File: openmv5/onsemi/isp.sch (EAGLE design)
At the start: 58 parts, among them IC1 AP0202AT2L00XPGA0, IC2 MIC5365-2.8YC5-TR, IC3 TLV62568PDDCR, J1 DF12-36-DS, J2 DF12-36-DP, M1 9774030151R, M2 9774030151R, Q1 PMXB120EPEZ

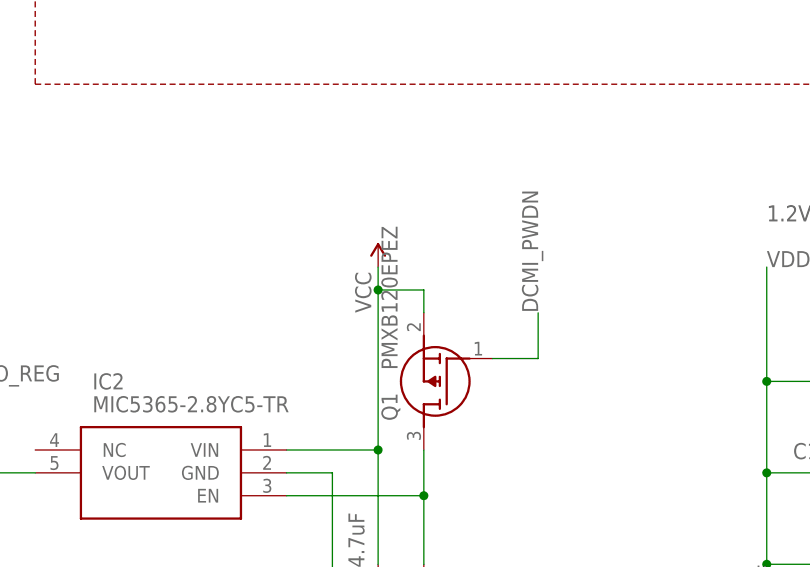
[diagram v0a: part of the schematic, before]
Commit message: Update camera modules to use different non-flippable pmosfet
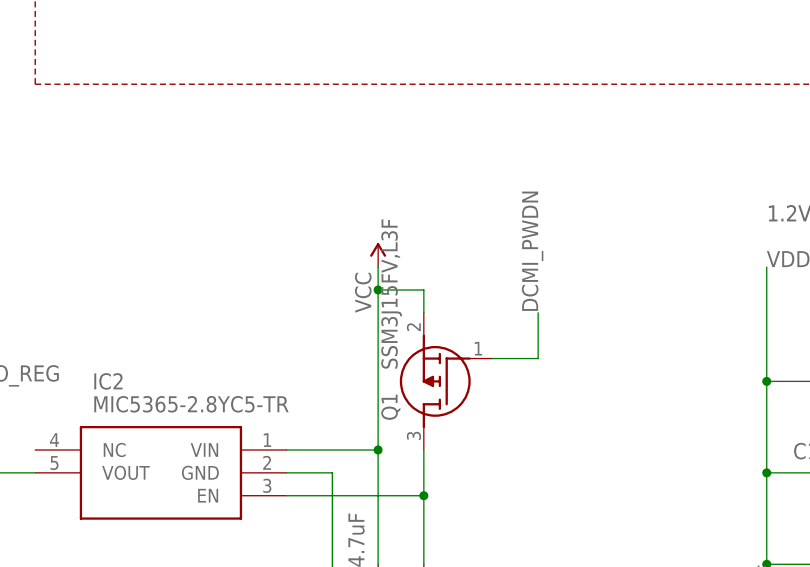
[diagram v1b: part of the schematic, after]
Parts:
- J1: MPN DF12NB-36DS-0.5V(51) -> DF12NB(3.0)-36DS-0.5V(51)
- Q1: value PMXB120EPEZ -> SSM3J15FV,L3F; device PMXB120EPEZ:PMXB120EPEZ -> SSM3J15FV_L3F:SSM3J15FV,L3F; MPN PMXB120EPEZ -> SSM3J15FV,L3F
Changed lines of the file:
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@@
 </part>
 <part name="GND11" library="supply" deviceset="GND" device=""/>
-<part name="Q1" library="PMXB120EPEZ" deviceset="PMXB120EPEZ" device="">
-<attribute name="MPN" value="PMXB120EPEZ"/>
+<part name="Q1" library="SSM3J15FV_L3F" deviceset="SSM3J15FV,L3F" device="">
+<attribute name="MPN" value="SSM3J15FV,L3F"/>
 </part>
 <part name="R5" library="rcl" library_urn="urn:adsk.eagle:library:334" deviceset="R-US_" device="R0402" package3d_urn="urn:adsk.eagle:package:23547/3" value="100K">
@@
 <part name="P+4" library="SparkFun" deviceset="VCC" device=""/>
 <part name="J1" library="DF12-36-DS" deviceset="DF12-36-DS" device="">
-<attribute name="MPN" value="DF12NB-36DS-0.5V(51)"/>
+<attribute name="MPN" value="DF12NB(3.0)-36DS-0.5V(51)"/>
 </part>
 <part name="GND2" library="SparkFun" deviceset="GND" device=""/>
